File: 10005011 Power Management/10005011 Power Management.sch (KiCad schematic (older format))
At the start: 0 parts

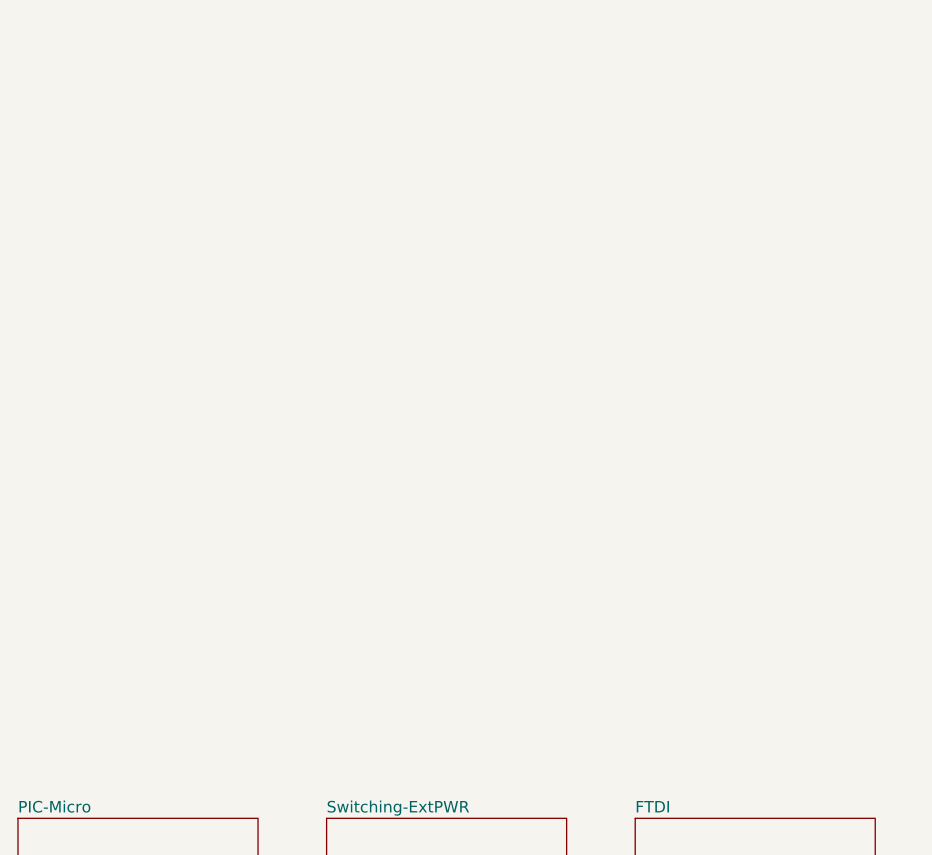
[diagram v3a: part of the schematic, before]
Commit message: change CR1-BIS to ZCR1 so that kicad does not think it is missing annotation, do the same in the PCB to be able to read netlist without components getting erased and placed new
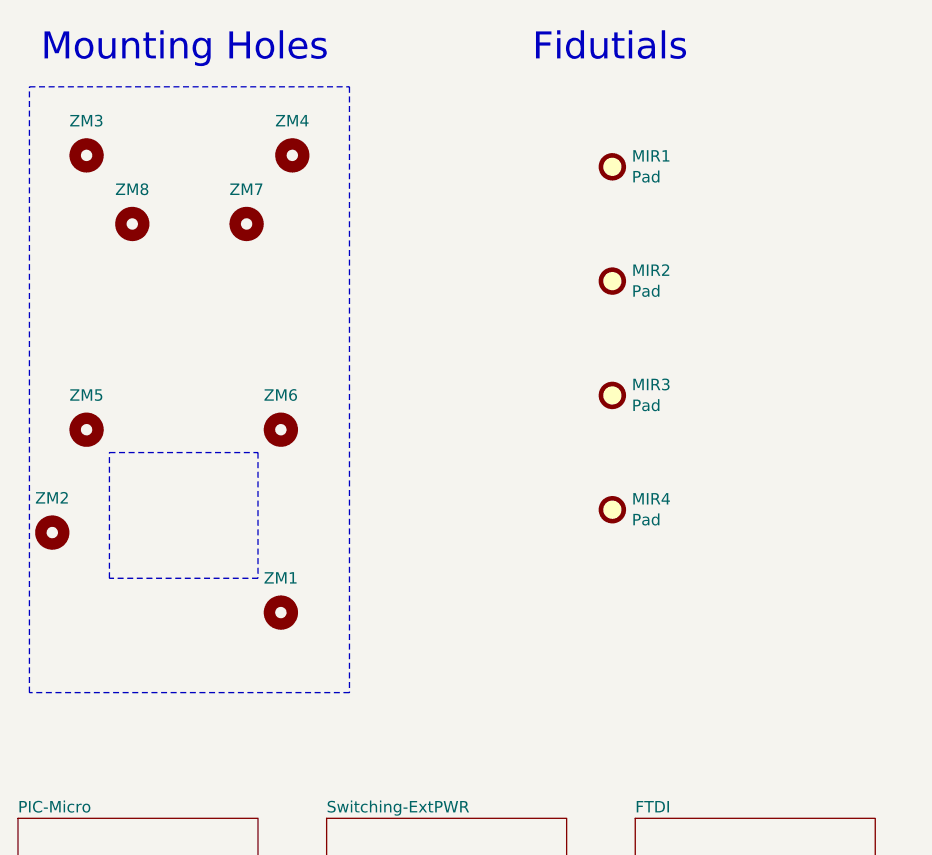
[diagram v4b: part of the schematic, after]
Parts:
- added MIR1, MIR2, MIR3, MIR4: Pad, 10005011 Power Management:MIRECMS_D-1.5_1, symbol Mechanical:Fiducial
- added ZM1, ZM2, ZM3, ZM4: MountingHole, 10005011 Power Management:FIX45_1, symbol Mechanical:MountingHole
- added ZM5, ZM6, ZM7, ZM8: MountingHole, 10005011 Power Management:FIX40_1, symbol Mechanical:MountingHole
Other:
- note added: "Fidutials"
- note added: "Mounting Holes"
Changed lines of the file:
@@
 Text Notes 1250 4700 0    118  ~ 0
 SHEET1
+$Comp
+L Mechanical:MountingHole ZM1
+U 1 1 5E973F3B
+P 2200 3350
+F 0 "ZM1" H 2200 3500 50  0000 C CNN
+F 1 "MountingHole" H 2300 3305 50  0001 L CNN
+F 2 "10005011 Power Management:FIX45_1" H 2200 3350 50  0001 C CNN
+F 3 "~" H 2200 3350 50  0001 C CNN
+	1    2200 3350
+	1    0    0    -1
+$EndComp
+$Comp
+L Mechanical:MountingHole ZM2
+U 1 1 5E974299
+P 1200 3000
+F 0 "ZM2" H 1200 3150 50  0000 C CNN
+F 1 "MountingHole" H 1300 2955 50  0001 L CNN
+F 2 "10005011 Power Management:FIX45_1" H 1200 3000 50  0001 C CNN
+F 3 "~" H 1200 3000 50  0001 C CNN
+	1    1200 3000
+	1    0    0    -1
+$EndComp
+$Comp
+L Mechanical:MountingHole ZM5
+U 1 1 5E974965
+P 1350 2550
+F 0 "ZM5" H 1350 2700 50  0000 C CNN
+F 1 "MountingHole" H 1450 2505 50  0001 L CNN
+F 2 "10005011 Power Management:FIX40_1" H 1350 2550 50  0001 C CNN
+F 3 "~" H 1350 2550 50  0001 C CNN
+	1    1350 2550
+	1    0    0    -1
+$EndComp
+$Comp
+L Mechanical:MountingHole ZM6
+U 1 1 5E97496F
+P 2200 2550
+F 0 "ZM6" H 2200 2700 50  0000 C CNN
+F 1 "MountingHole" H 2300 2505 50  0001 L CNN
+F 2 "10005011 Power Management:FIX40_1" H 2200 2550 50  0001 C CNN
+F 3 "~" H 2200 2550 50  0001 C CNN
+	1    2200 2550
+	1    0    0    -1
+$EndComp
+$Comp
+L Mechanical:MountingHole ZM3
+U 1 1 5E97529B
+P 1350 1350
+F 0 "ZM3" H 1350 1500 50  0000 C CNN
+F 1 "MountingHole" H 1450 1305 50  0001 L CNN
+F 2 "10005011 Power Management:FIX45_1" H 1350 1350 50  0001 C CNN
+F 3 "~" H 1350 1350 50  0001 C CNN
+	1    1350 1350
+	1    0    0    -1
+$EndComp
+$Comp
+L Mechanical:MountingHole ZM4
+U 1 1 5E9752A5
+P 2250 1350
+F 0 "ZM4" H 2250 1500 50  0000 C CNN
+F 1 "MountingHole" H 2350 1305 50  0001 L CNN
+F 2 "10005011 Power Management:FIX45_1" H 2250 1350 50  0001 C CNN
+F 3 "~" H 2250 1350 50  0001 C CNN
+	1    2250 1350
+	1    0    0    -1
+$EndComp
+$Comp
+L Mechanical:MountingHole ZM7
+U 1 1 5E9752AF
+P 2050 1650
+F 0 "ZM7" H 2050 1800 50  0000 C CNN
+F 1 "MountingHole" H 2150 1605 50  0001 L CNN
+F 2 "10005011 Power Management:FIX40_1" H 2050 1650 50  0001 C CNN
+F 3 "~" H 2050 1650 50  0001 C CNN
+	1    2050 1650
+	1    0    0    -1
+$EndComp
+$Comp
+L Mechanical:MountingHole ZM8
+U 1 1 5E9752B9
+P 1550 1650
+F 0 "ZM8" H 1550 1800 50  0000 C CNN
+F 1 "MountingHole" H 1650 1605 50  0001 L CNN
+F 2 "10005011 Power Management:FIX40_1" H 1550 1650 50  0001 C CNN
+F 3 "~" H 1550 1650 50  0001 C CNN
+	1    1550 1650
+	1    0    0    -1
+$EndComp
+$Comp
+L Mechanical:Fiducial MIR3
+U 1 1 5EA84F61
+P 3650 2400
+F 0 "MIR3" H 3735 2446 50  0000 L CNN
+F 1 "Pad" H 3735 2355 50  0000 L CNN
+F 2 "10005011 Power Management:MIRECMS_D-1.5_1" H 3850 2400 50  0001 C CNN
+F 3 "~" H 3850 2400 50  0001 C CNN
+	1    3650 2400
+	1    0    0    -1
+$EndComp
+$Comp
+L Mechanical:Fiducial MIR4
+U 1 1 5EA8549D
+P 3650 2900
+F 0 "MIR4" H 3735 2946 50  0000 L CNN
+F 1 "Pad" H 3735 2855 50  0000 L CNN
+F 2 "10005011 Power Management:MIRECMS_D-1.5_1" H 3850 2900 50  0001 C CNN
+F 3 "~" H 3850 2900 50  0001 C CNN
+	1    3650 2900
+	1    0    0    -1
+$EndComp
+Wire Notes Line
+	1100 1050 2500 1050
+Wire Notes Line
+	2500 1050 2500 3700
+Wire Notes Line
+	2500 3700 1100 3700
+Wire Notes Line
+	1100 3700 1100 1050
+Wire Notes Line
+	1450 2650 2100 2650
+Wire Notes Line
+	2100 2650 2100 3200
+Wire Notes Line
+	2100 3200 1450 3200
+Wire Notes Line
+	1450 3200 1450 2650
+$Comp
+L Mechanical:Fiducial MIR2
+U 1 1 5EA84D93
+P 3650 1900
+F 0 "MIR2" H 3735 1946 50  0000 L CNN
+F 1 "Pad" H 3735 1855 50  0000 L CNN
+F 2 "10005011 Power Management:MIRECMS_D-1.5_1" H 3850 1900 50  0001 C CNN
+F 3 "~" H 3850 1900 50  0001 C CNN
+	1    3650 1900
+	1    0    0    -1
+$EndComp
+$Comp
+L Mechanical:Fiducial MIR1
+U 1 1 5EA84054
+P 3650 1400
+F 0 "MIR1" H 3735 1446 50  0000 L CNN
+F 1 "Pad" H 3735 1355 50  0000 L CNN
+F 2 "10005011 Power Management:MIRECMS_D-1.5_1" H 3850 1400 50  0001 C CNN
+F 3 "~" H 3850 1400 50  0001 C CNN
+	1    3650 1400
+	1    0    0    -1
+$EndComp
+Text Notes 1150 950  0    118  ~ 0
+Mounting Holes
+Text Notes 3300 950  0    118  ~ 0
+Fidutials
 $EndSCHEMATC

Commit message: add all 3D models
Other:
- note added: "Fiducials"
- note removed: "Fidutials"
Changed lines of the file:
@@
 Mounting Holes
 Text Notes 3300 950  0    118  ~ 0
-Fidutials
+Fiducials
 $EndSCHEMATC

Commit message: Powermanagement dev, ERC
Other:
- note added: "Power Flags for ERC"
- note added: "There are more power flags on sheets 2, 3, 6, and 7"

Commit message: update fp path
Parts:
- MIR1, MIR2, MIR3, MIR4: footprint 10005011 Power Management:MIRECMS_D-1.5_1 -> AllModules:MIRECMS_D-1.5_1
- ZM1, ZM2, ZM3, ZM4: footprint 10005011 Power Management:FIX45_1 -> AllModules:FIX45_1
- ZM5, ZM6, ZM7, ZM8: footprint 10005011 Power Management:FIX40_1 -> AllModules:FIX40_1
